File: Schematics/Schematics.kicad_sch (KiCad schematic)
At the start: 15 parts, among them SW1 SW_MEC_5E, U1 74HC595, U2 CC56-12YWA

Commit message: Final Kicad changes
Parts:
- added BT1: Battery_Cell, symbol Device:Battery_Cell
- added SW2: SW_DPDT_x2, Button_Switch_THT:SW_CuK_JS202011CQN_DPDT_Straight, symbol Switch:SW_DPDT_x2
- D1: value Green LED -> Green
- D2: value Orange LED -> Orange
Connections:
- net GND: now also D2.1 (K); no longer A1.29 (GND)
- net Dat2: now reaches A1.6 (D3), R5.1
- net Dat3: now reaches A1.7 (D4), R7.1
- net Dat1: now reaches A1.5 (D2), R8.1
- net at A1.10 (D7): now also SW1.4 (A); no longer SW1.3 (K)
- net at A1.4 (GND): no longer D2.1 (K)
- net Dat4: now reaches A1.8 (D5), R6.1
- net +9V: no longer names the net of A1.30 (VIN)
- net +9V: now also SW2.3 (C)
- new net: BT1.1 (+), SW2.2 (B)
- new net BT GND: A1.29 (GND), BT1.2 (-)
- no-connect marks 1 -> 20
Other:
- note added: "15-01-2021"
- note added: "Pomodoro Device"
- moved on the sheet: R5, R6, R7, R8

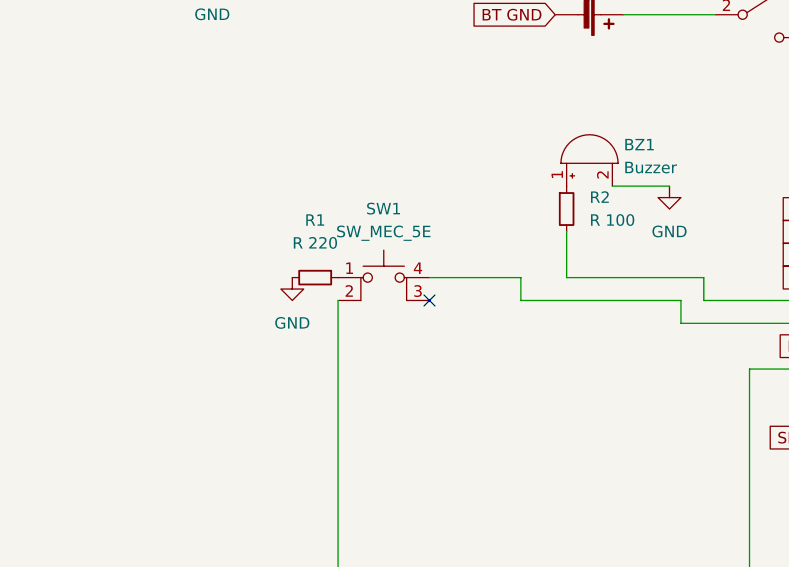
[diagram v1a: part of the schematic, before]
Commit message: new fucntion in device
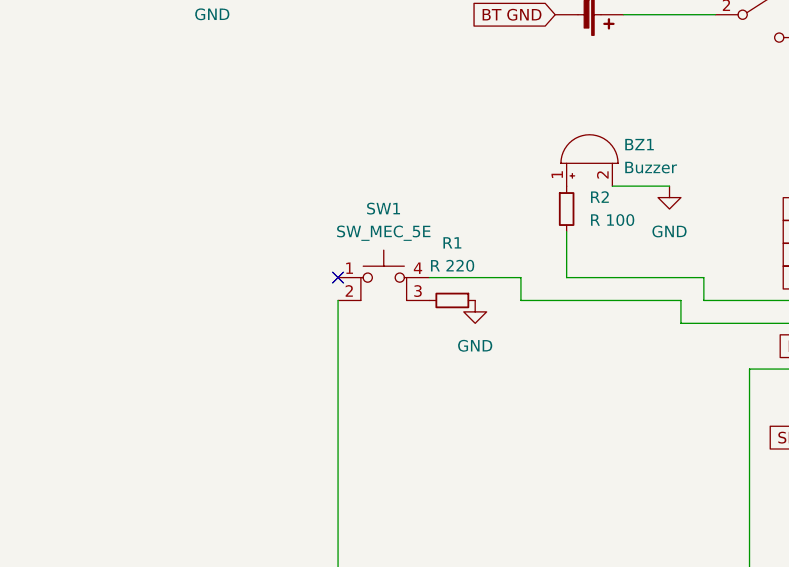
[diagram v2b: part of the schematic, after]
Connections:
- net GND: now also R1.1; no longer R1.2
- net at SW1.1: no longer R1.1
- net at SW1.3 (K): now also R1.2
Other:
- moved on the sheet: R1
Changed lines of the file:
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@@
   (junction (at 170.18 95.25) (diameter 0) (color 0 0 0 0)
   )
-  (no_connect (at 106.68 120.65))
+  (no_connect (at 96.52 118.11))
   (no_connect (at 152.4 105.41))
   (no_connect (at 152.4 107.95))
@@
   )
   (symbol (lib_id "Device:R_Small") (at 121.92 110.49 0) (unit 1)
-    (in_bom yes) (on_board yes) (fields_autoplaced)
+    (in_bom yes) (on_board yes)
     (property "Reference" "R2" (id 0) (at 124.46 109.2199 0)
       (effects (font (size 1.27 1.27)) (justify left))
@@
     (pin "4")
   )
-  (symbol (lib_id "Device:R_Small") (at 93.98 118.11 270) (unit 1)
-    (in_bom yes) (on_board yes) (fields_autoplaced)
-    (property "Reference" "R1" (id 0) (at 93.98 111.76 90))
-    (property "Value" "R 220" (id 1) (at 93.98 114.3 90))
-    (property "Footprint" "Resistor_THT:R_Axial_DIN0309_L9.0mm_D3.2mm_P12.70mm_Horizontal" (id 2) (at 93.98 118.11 0)
-      (effects (font (size 1.27 1.27)) hide)
-    )
-    (property "Datasheet" "~" (id 3) (at 93.98 118.11 0)
+  (symbol (lib_id "Device:R_Small") (at 109.22 120.65 270) (unit 1)
+    (in_bom yes) (on_board yes) (fields_autoplaced)
+    (property "Reference" "R1" (id 0) (at 109.22 114.3 90))
+    (property "Value" "R 220" (id 1) (at 109.22 116.84 90))
+    (property "Footprint" "Resistor_THT:R_Axial_DIN0309_L9.0mm_D3.2mm_P12.70mm_Horizontal" (id 2) (at 109.22 120.65 0)
+      (effects (font (size 1.27 1.27)) hide)
+    )
+    (property "Datasheet" "~" (id 3) (at 109.22 120.65 0)
       (effects (font (size 1.27 1.27)) hide)
     )
@@
     (pin "2")
   )
-  (symbol (lib_id "power:GND") (at 91.44 118.11 0) (unit 1)
-    (in_bom yes) (on_board yes) (fields_autoplaced)
-    (property "Reference" "#PWR03" (id 0) (at 91.44 124.46 0)
-      (effects (font (size 1.27 1.27)) hide)
-    )
-    (property "Value" "GND" (id 1) (at 91.44 123.19 0))
-    (property "Footprint" "" (id 2) (at 91.44 118.11 0)
-      (effects (font (size 1.27 1.27)) hide)
-    )
-    (property "Datasheet" "" (id 3) (at 91.44 118.11 0)
-      (effects (font (size 1.27 1.27)) hide)
-    )
+  (symbol (lib_id "power:GND") (at 111.76 120.65 0) (unit 1)
+    (in_bom yes) (on_board yes) (fields_autoplaced)
+    (property "Reference" "#PWR03" (id 0) (at 111.76 127 0)
+      (effects (font (size 1.27 1.27)) hide)
+    )
+    (property "Value" "GND" (id 1) (at 111.76 125.73 0))
+    (property "Footprint" "" (id 2) (at 111.76 120.65 0)
+      (effects (font (size 1.27 1.27)) hide)
+    )
+    (property "Datasheet" "" (id 3) (at 111.76 120.65 0)
+      (effects (font (size 1.27 1.27)) hide)
+    )
